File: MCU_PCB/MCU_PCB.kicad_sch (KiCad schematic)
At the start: 0 parts

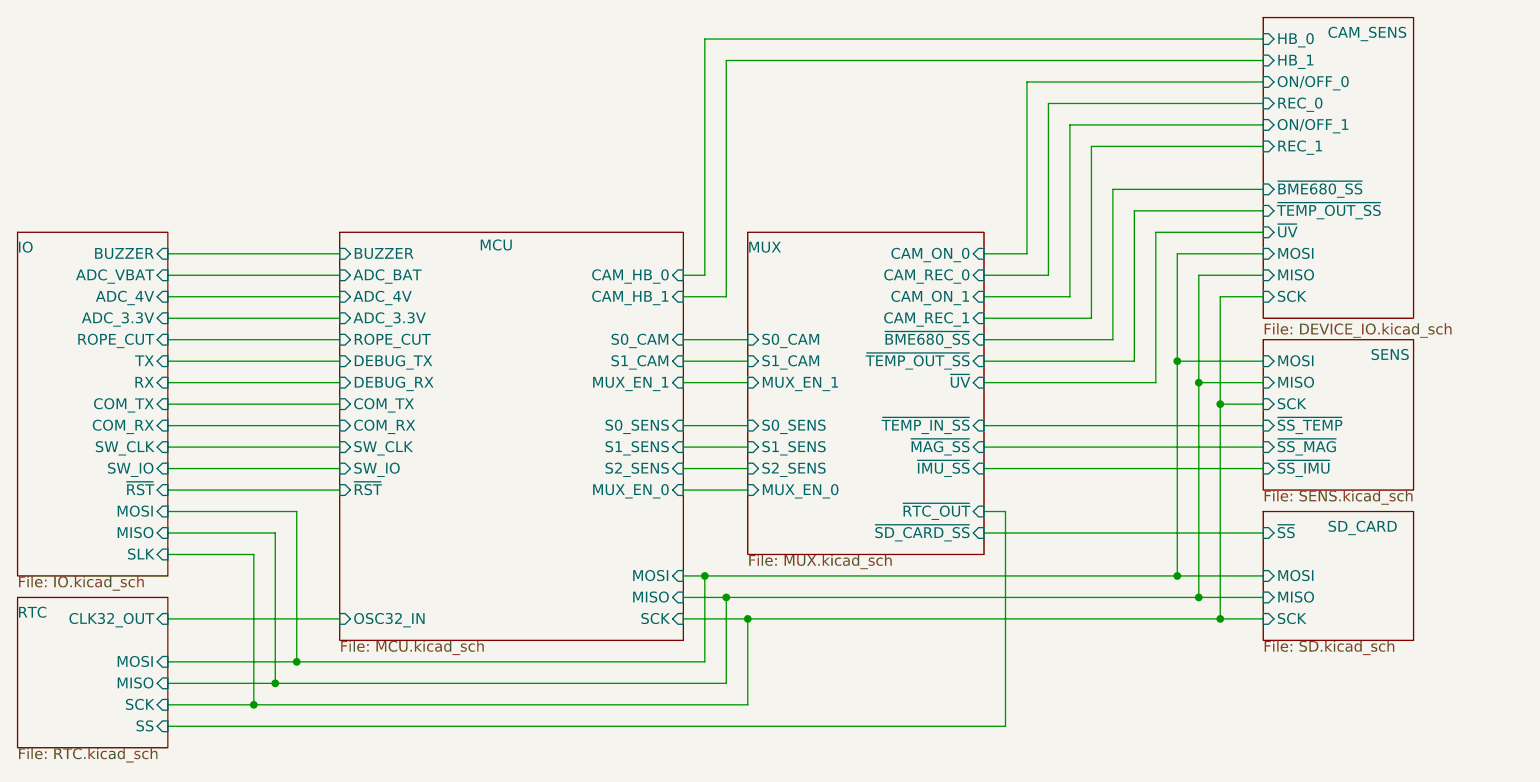
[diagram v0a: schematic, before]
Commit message: 0.1v MCU KiCad
Aesthetics needs to be improved.
Trace width needs to be changed.
More sufficient grounding.
Component placement could be changed.
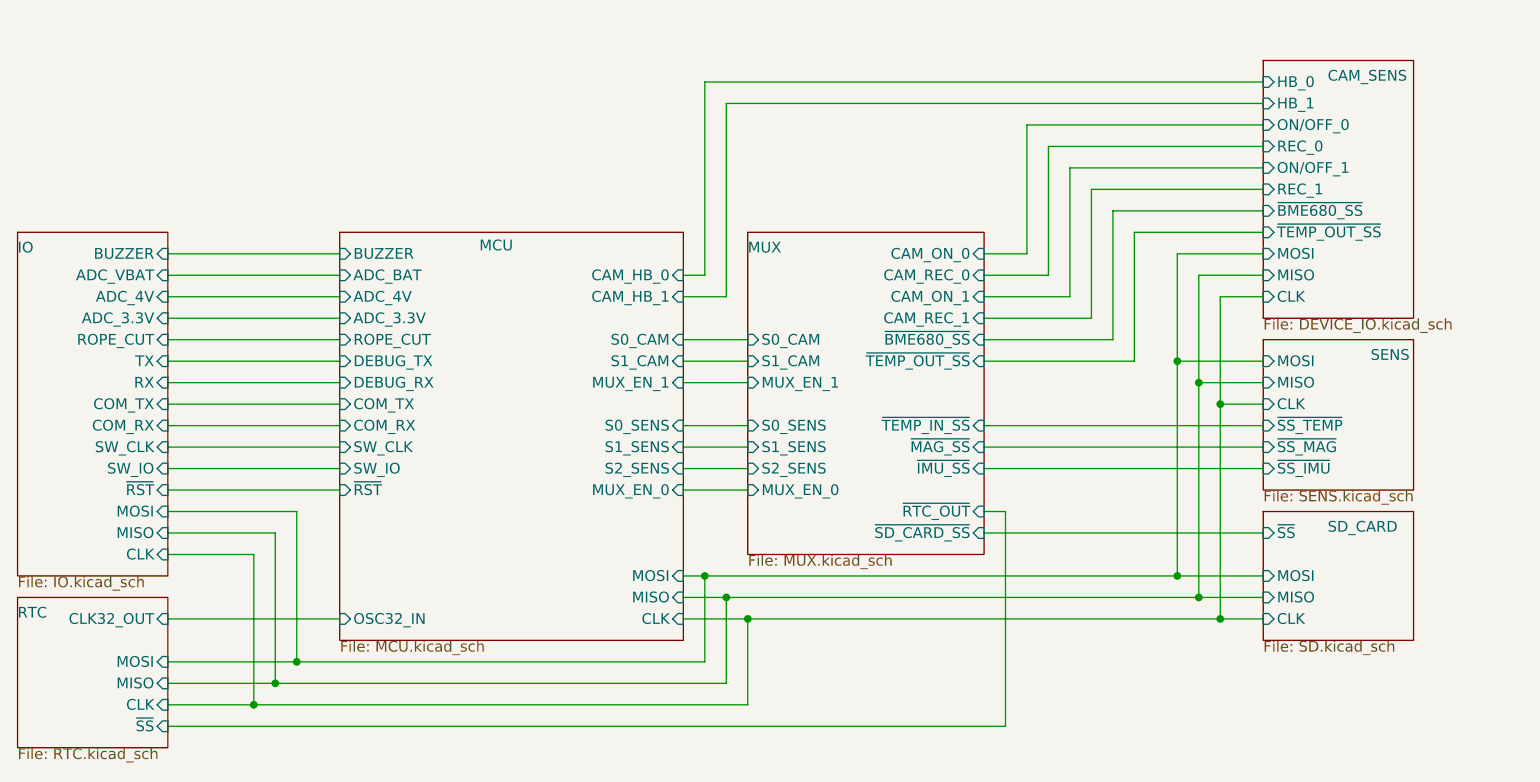
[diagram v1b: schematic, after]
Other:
- sheet CAM_SENS ports: added CLK; removed SCK, ~{UV}
- sheet IO ports: added CLK; removed SLK
- sheet MCU ports: added CLK; removed SCK
- sheet MUX ports: added none; removed ~{UV}
- sheet RTC ports: added CLK, ~{SS}; removed SCK, SS
- sheet SD_CARD ports: added CLK; removed SCK
- sheet SENS ports: added CLK; removed SCK
